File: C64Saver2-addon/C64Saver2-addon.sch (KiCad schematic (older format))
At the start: 37 parts, among them J1 Conn_01x08_Female, J2 Conn_01x08_Female, J3 OLED_128x32_Conn_01x04_Male, J4 Conn_01x04_Female, SW1 SW_Push, U1 INA219xIDR-SOIC, U2 ISO1541D, U3 ATTINY85-20SU, U4 TLP291, U5 TLP291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

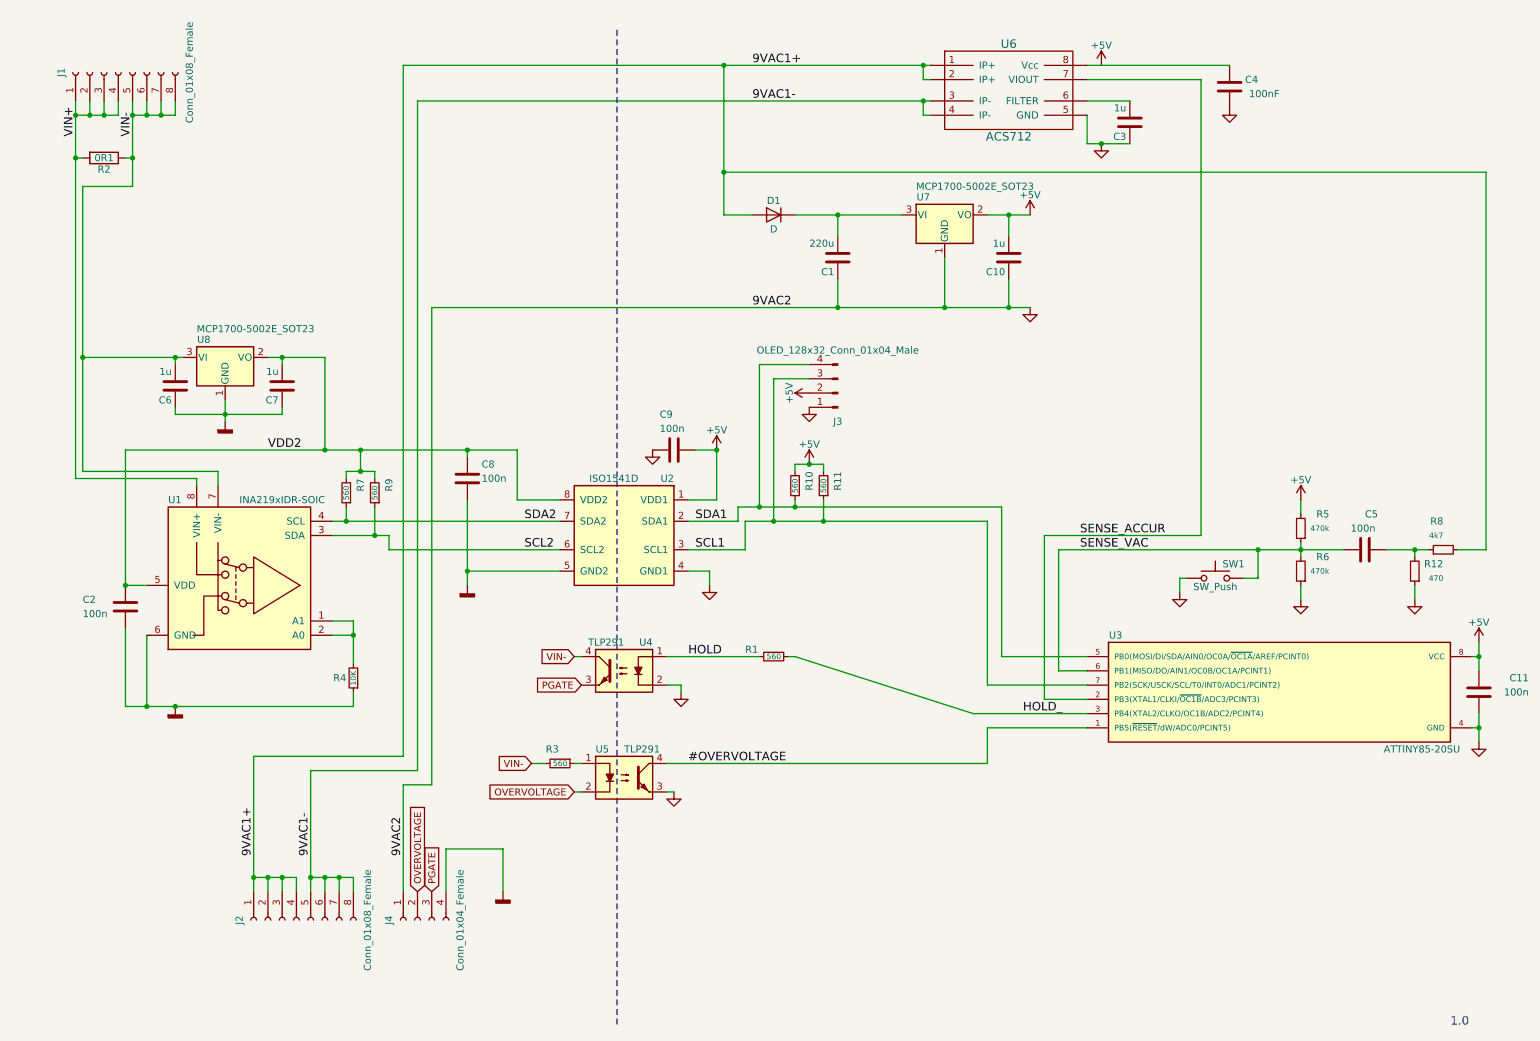
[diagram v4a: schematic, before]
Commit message: addon board component placement done. layout begun.
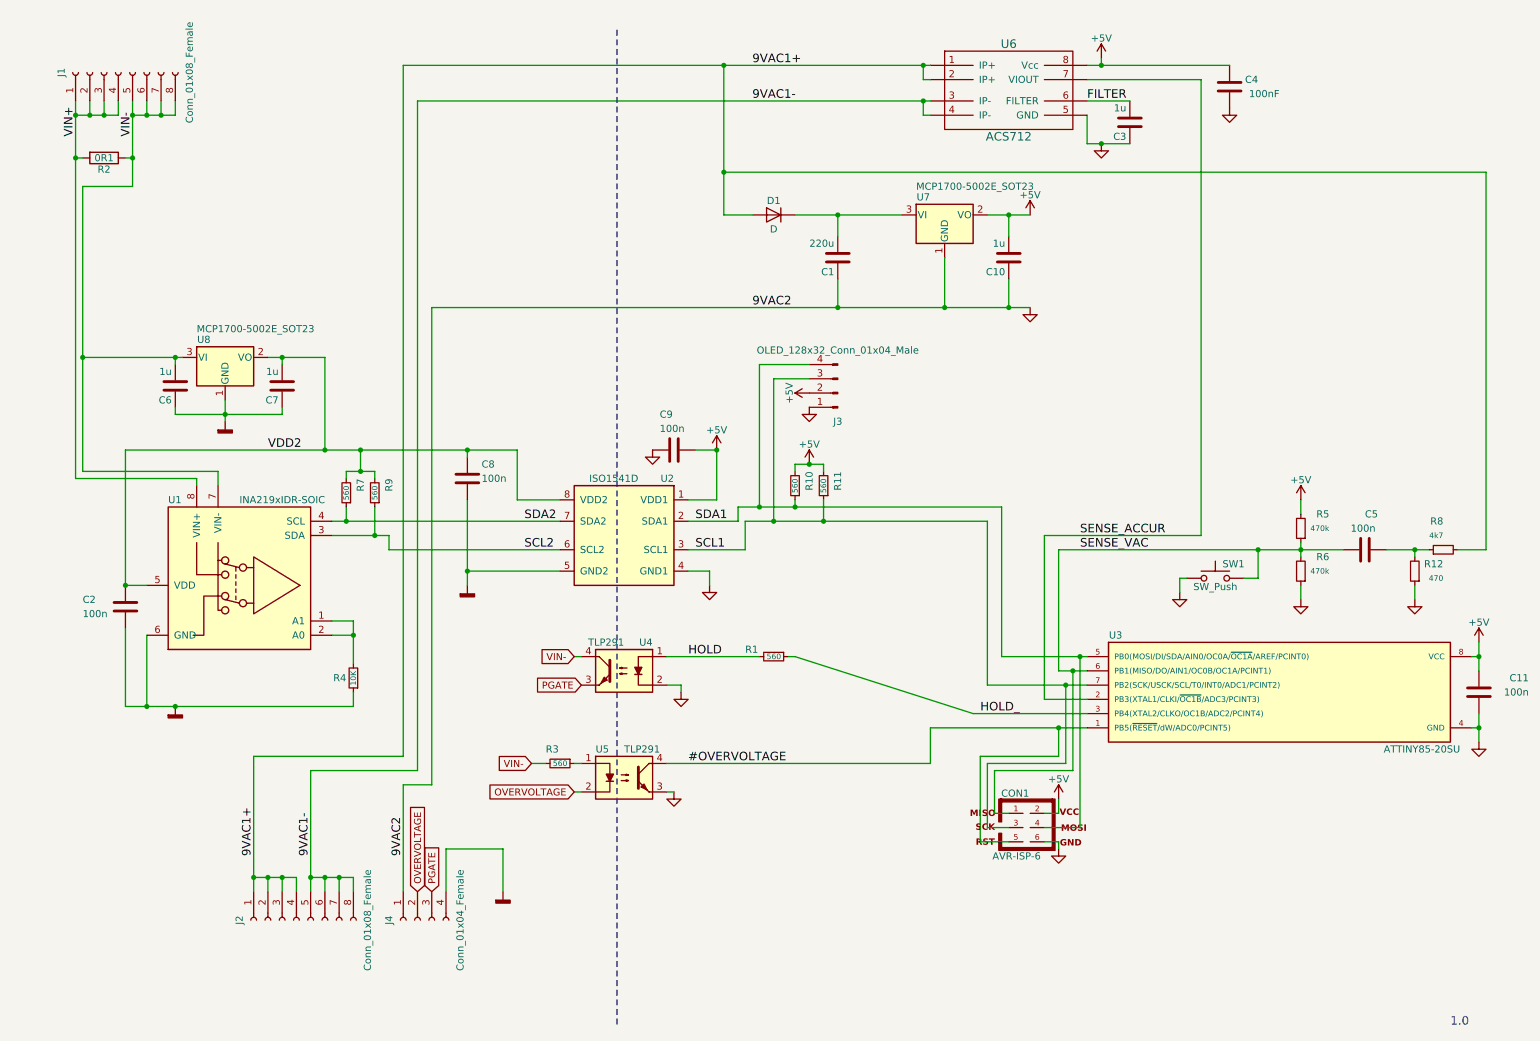
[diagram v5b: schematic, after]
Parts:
- added CON1: AVR-ISP-6, Pin_Headers:Pin_Header_Straight_2x03_Pitch2.00mm, symbol AVR-ISP-6
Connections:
- net #OVERVOLTAGE: now also CON1.5
- net +5V: now also C4.2, U6.8 (Vcc), CON1.2
- net GND: now also CON1.6
- net SCL1: now also CON1.3
- net SDA1: now also CON1.4
- net SENSE_VAC: now also CON1.1
- net FILTER: now reaches C3.2, U6.6 (FILTER)
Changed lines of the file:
@@
 L +5V #PWR05
 U 1 1 5B2ADC33
-P 8200 900
-F 0 "#PWR05" H 8200 750 50  0001 C CNN
-F 1 "+5V" H 8200 1040 50  0000 C CNN
-F 2 "" H 8200 900 50  0001 C CNN
-F 3 "" H 8200 900 50  0001 C CNN
-	1    8200 900
+P 8200 850
+F 0 "#PWR05" H 8200 700 50  0001 C CNN
+F 1 "+5V" H 8200 990 50  0000 C CNN
+F 2 "" H 8200 850 50  0001 C CNN
+F 3 "" H 8200 850 50  0001 C CNN
+	1    8200 850
 	1    0    0    -1
 $EndComp
@@
 	1    0    0    -1
 $EndComp
-Text Label 7650 5450 0    60   ~ 0
+Text Label 7350 5450 0    60   ~ 0
 HOLD_
 $Comp
@@
 	5150 6000 5200 6000
 Wire Wire Line
-	5150 5800 7400 5800
+	5150 5800 7000 5800
 Wire Wire Line
 	2950 5400 2950 5300
@@
 	6050 5050 6000 5050
 Wire Wire Line
-	8100 5150 7900 5150
+	7900 5150 8100 5150
 Wire Wire Line
 	7900 5150 7900 4300
@@
 	10400 4650 10400 4550
 Wire Wire Line
-	10500 4300 10200 4300
+	10200 4300 10500 4300
 Wire Wire Line
 	7900 4300 9900 4300
@@
 	7400 5250 7400 4100
 Wire Wire Line
-	8100 5050 7500 5050
-Wire Wire Line
-	7500 5050 7500 4000
-Wire Wire Line
-	7400 5800 7400 5550
-Wire Wire Line
-	7400 5550 8100 5550
+	7500 5050 8100 5050
+Wire Wire Line
+	7500 4000 7500 5050
+Wire Wire Line
+	7000 5800 7000 5550
+Wire Wire Line
+	7000 5550 8100 5550
 Wire Wire Line
 	9200 4500 9300 4500
@@
 $EndComp
 Wire Wire Line
-	10850 5650 10850 5450
+	10850 5450 10850 5650
 Wire Wire Line
 	10800 5550 10850 5550
 Connection ~ 10850 5550
 Wire Wire Line
-	10850 5150 10850 4950
+	10850 4950 10850 5150
 Wire Wire Line
 	10800 5050 10850 5050
 Connection ~ 10850 5050
+$Comp
+L AVR-ISP-6 CON1
+U 1 1 5B45B072
+P 7700 6250
+F 0 "CON1" H 7595 6490 50  0000 C CNN
+F 1 "AVR-ISP-6" H 7435 6020 50  0000 L BNN
+F 2 "Pin_Headers:Pin_Header_Straight_2x03_Pitch2.00mm" V 7180 6290 50  0001 C CNN
+F 3 "" H 7675 6250 50  0001 C CNN
+	1    7700 6250
+	1    0    0    -1
+$EndComp
+$Comp
+L GND #PWR024
+U 1 1 5B45B7CD
+P 7900 6400
+F 0 "#PWR024" H 7900 6150 50  0001 C CNN
+F 1 "GND" H 7900 6250 50  0001 C CNN
+F 2 "" H 7900 6400 50  0001 C CNN
+F 3 "" H 7900 6400 50  0001 C CNN
+	1    7900 6400
+	1    0    0    -1
+$EndComp
+Wire Wire Line
+	7900 6400 7900 6350
+Wire Wire Line
+	7900 6350 7800 6350
+$Comp
+L +5V #PWR025
+U 1 1 5B45C11F
+P 7900 6050
+F 0 "#PWR025" H 7900 5900 50  0001 C CNN
+F 1 "+5V" H 7900 6190 50  0000 C CNN
+F 2 "" H 7900 6050 50  0001 C CNN
+F 3 "" H 7900 6050 50  0001 C CNN
+	1    7900 6050
+	1    0    0    -1
+$EndComp
+Wire Wire Line
+	7900 6050 7900 6150
+Wire Wire Line
+	7900 6150 7800 6150
+Wire Wire Line
+	7800 6250 8050 6250
+Wire Wire Line
+	8050 6250 8050 5050
+Connection ~ 8050 5050
+Wire Wire Line
+	7550 6150 7450 6150
+Wire Wire Line
+	7450 6150 7450 5850
+Wire Wire Line
+	7450 5850 8000 5850
+Wire Wire Line
+	8000 5850 8000 5150
+Connection ~ 8000 5150
+Wire Wire Line
+	7550 6250 7400 6250
+Wire Wire Line
+	7400 6250 7400 5800
+Wire Wire Line
+	7400 5800 7950 5800
+Wire Wire Line
+	7950 5800 7950 5250
+Connection ~ 7950 5250
+Wire Wire Line
+	7550 6350 7350 6350
+Wire Wire Line
+	7350 6350 7350 5750
+Wire Wire Line
+	7350 5750 7900 5750
+Wire Wire Line
+	7900 5750 7900 5550
+Connection ~ 7900 5550
+Wire Wire Line
+	8200 850  8200 900
+Connection ~ 8200 900
+Text Label 8100 1150 0    60   ~ 0
+FILTER
 $EndSCHEMATC
